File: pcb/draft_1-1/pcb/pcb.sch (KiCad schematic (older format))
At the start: 23 parts, among them J1 USB4110-GF-A, U1 H3LIS200DLTR, U2 ATSAML21G16B-AUT, U3 BQ25155

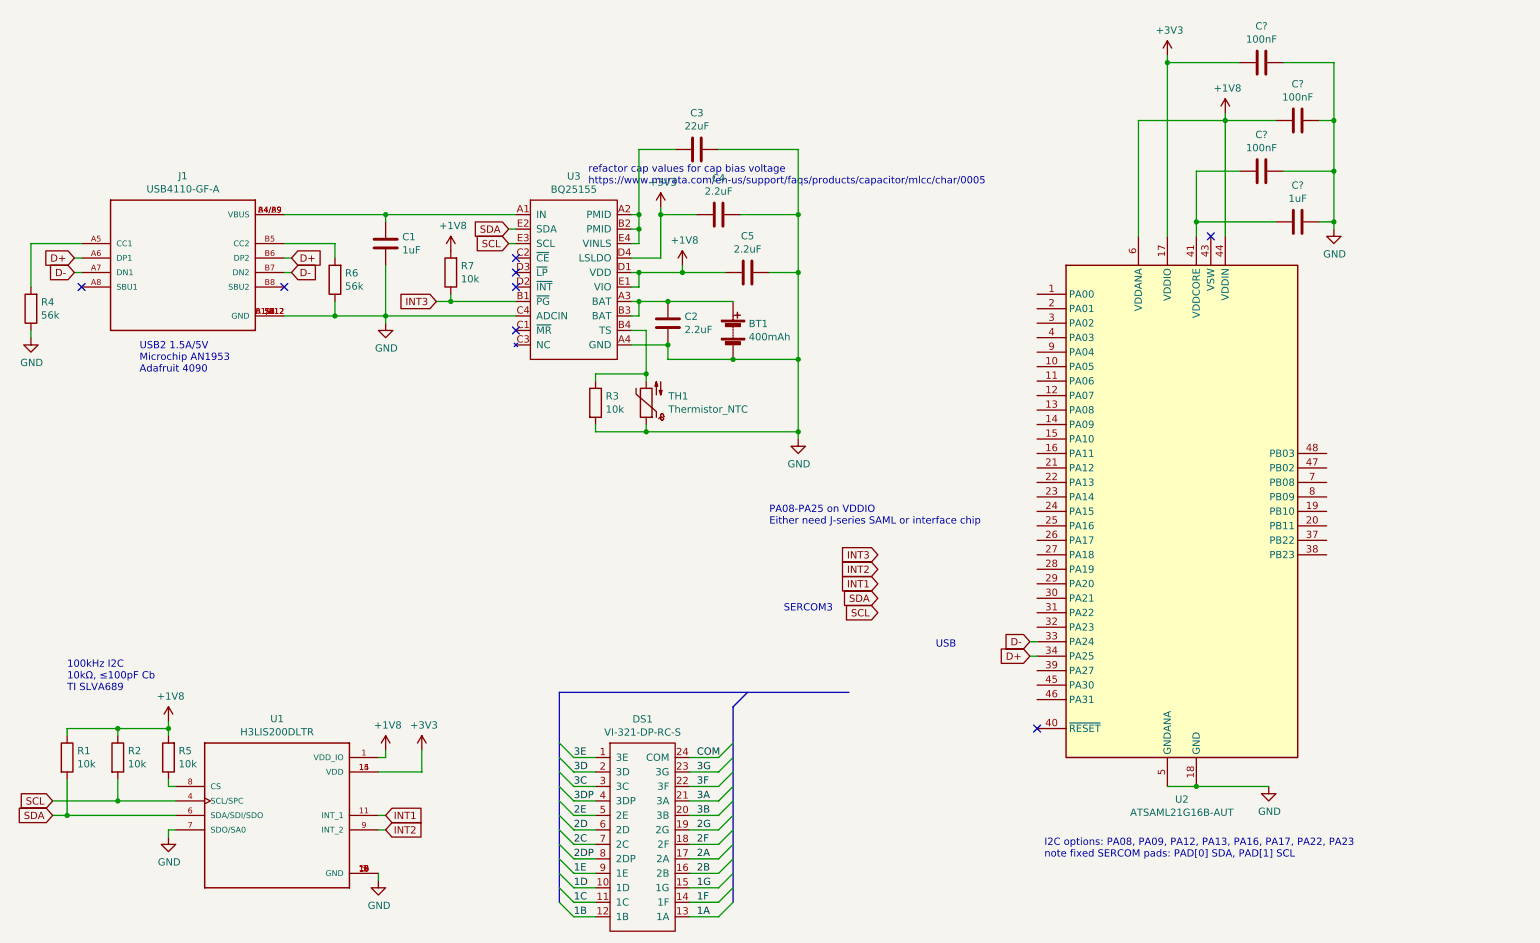
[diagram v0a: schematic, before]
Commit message: PRE-TRACE PLACEMENT CHECKPOINT
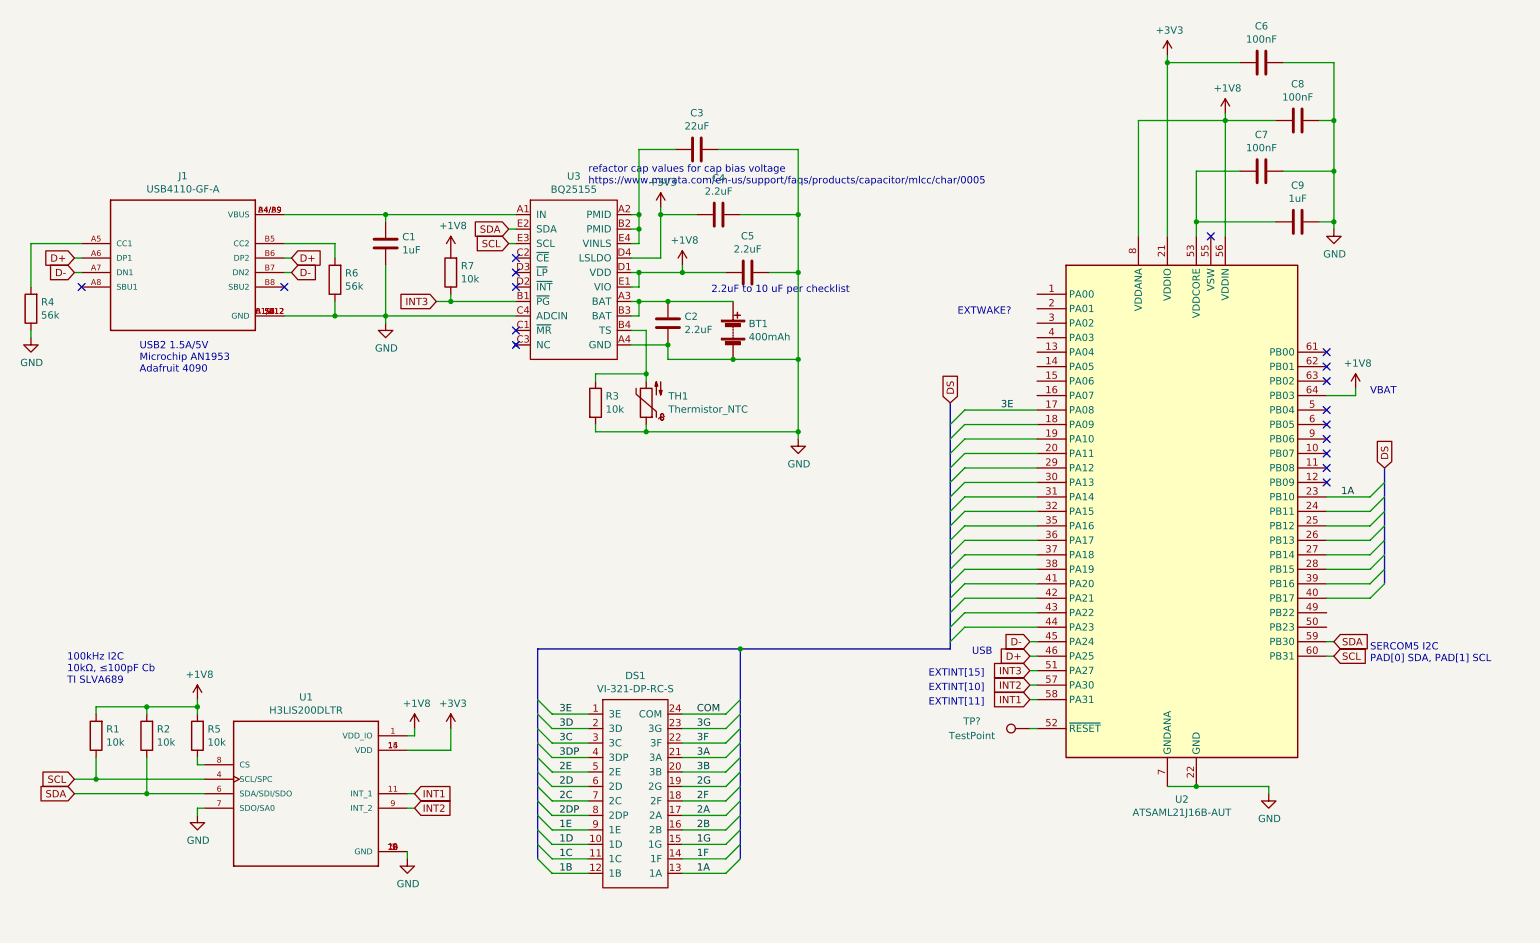
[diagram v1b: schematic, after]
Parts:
- removed U2: ATSAML21G16B-AUT, Package_QFP:TQFP-48_7x7mm_P0.5mm, symbol MCU_Microchip_SAML:ATSAML21G16B-AUT
- added TP?: TestPoint, symbol Connector:TestPoint
- added U2: ATSAML21J16B-AUT, Package_QFP:TQFP-64_10x10mm_P0.5mm, symbol MCU_Microchip_SAML:ATSAML21J16B-AUT
- DS1: footprint (none) -> custom:VI-321-DP-RC-S
- U3: footprint (none) -> SamacSys_Parts:BGA20C40P4X5_162X202X50
- gave numbers to parts that had none: 4
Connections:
- net +1V8: now also R1.2, R2.2, U2.56 (VDDIN), U2.64 (PB03), U2.8 (VDDANA); no longer R1.1, R2.1
- net +3V3: now also U2.21 (VDDIO), U2.34 (VDDIO), U2.48 (VDDIO)
- net 1A: now also U2.23 (PB10)
- net 3E: now also U2.17 (PA08)
- net D+: now also U2.46 (PA25)
- net D-: now also U2.45 (PA24)
- net GND: now also U2.22 (GND), U2.33 (GND), U2.47 (GND), U2.54 (GND), U2.7 (GNDANA)
- net INT1: now also U2.58 (PA31)
- net INT2: now also U2.57 (PA30)
- net INT3: now also U2.51 (PA27)
- net SCL: now also R1.1, U2.60 (PB31); no longer R2.2
- net SDA: now also R2.1, U2.59 (PB30); no longer R1.2
- net at C7.1, C9.1: now also U2.53 (VDDCORE)
- new net: TP?.1, U2.52 (~RESET)
- no-connect marks 8 -> 17
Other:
- note added: "2.2uF to 10 uF per checklist"
- note added: "EXTINT[10]"
- note added: "EXTINT[11]"
- note added: "EXTINT[15]"
- note added: "EXTWAKE?"
- note added: "SERCOM5 I2C\nPAD[0] SDA, PAD[1] SCL"
- note added: "VBAT"
- note removed: "I2C options: PA08, PA09, PA12, PA13, PA16, PA17, PA22, PA23\nnote fixed SERCOM pads: PAD[0] SDA, PAD[1] SCL"
- note removed: "PA08-PA25 on VDDIO\nEither need J-series SAML or interface chip"
- note removed: "SERCOM3"
- moved on the sheet: DS1, R5, U1

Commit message: attempt to route display
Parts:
- removed TP?: TestPoint, symbol Connector:TestPoint
- added L1: 10uH, Inductor_SMD:L_0805_2012Metric, symbol Device:L
- C1, C2, C3, C4, C5, C6, C7, C8, C9: footprint (none) -> Capacitor_SMD:C_0402_1005Metric
- R1, R2, R3, R4, R5, R6, R7, TH1: footprint (none) -> Resistor_SMD:R_0402_1005Metric
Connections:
- net +3V3 is gone; now on net +1V8: C4.1, C6.1, U1.14 (VDD), U1.15 (VDD), U2.21 (VDDIO), U2.34 (VDDIO), U2.48 (VDDIO), U3.D4 (LSLDO)
- net 1B is gone; now on net 24: DS1.12 (1B)
- net 1C is gone; now on net 23: DS1.11 (1C)
- net 1D is gone; now on net 22: DS1.10 (1D)
- net 1E is gone; now on net 21: DS1.9 (1E)
- net 1F is gone; now on net 2: DS1.14 (1F)
- net 1G is gone; now on net 3: DS1.15 (1G)
- net 2B is gone; now on net 4: DS1.16 (2B)
- net 2C is gone; now on net 19: DS1.7 (2C)
- net 2D is gone; now on net 18: DS1.6 (2D)
- net 2DP is gone; now on net 20: DS1.8 (2DP)
- net 2E is gone; now on net 17: DS1.5 (2E)
- net 2F is gone; now on net 6: DS1.18 (2F)
- net 2G is gone; now on net 7: DS1.19 (2G)
- net 3A is gone; now on net 9: DS1.21 (3A)
- net 3B is gone; now on net 8: DS1.20 (3B)
- net 3C is gone; now on net 15: DS1.3 (3C)
- net 3D is gone; now on net 14: DS1.2 (3D)
- net 3DP is gone; now on net 16: DS1.4 (3DP)
- net 3F is gone; now on net 10: DS1.22 (3F)
- net 3G is gone; now on net 11: DS1.23 (3G)
- net COM is gone; now on net 12: DS1.24 (COM)
- net INT1: now also U2.16 (PA07); no longer U2.58 (PA31)
- net INT2: now also U2.15 (PA06); no longer U2.57 (PA30)
- net INT3: now also U2.14 (PA05); no longer U2.51 (PA27)
- net +5V: now reaches C1.1, J1.A4/B9 (VBUS), J1.B4/A9 (VBUS), U3.A1 (IN)
- net at C7.1, C9.1, U2.53 (VDDCORE): now also L1.1
- net 2: now reaches U2.18 (PA09)
- net 3: now reaches U2.19 (PA10)
- net 4: now reaches U2.20 (PA11)
- net 6: now reaches U2.24 (PB11)
- net 7: now reaches U2.25 (PB12)
- net 8: now reaches U2.26 (PB13)
- net 9: now reaches U2.27 (PB14)
- net 10: now reaches U2.28 (PB15)
- net 11: now reaches U2.29 (PA12)
- net 12: now reaches U2.30 (PA13)
- net 13: now reaches U2.31 (PA14)
- net 13: now also DS1.1 (3E)
- net 14: now reaches U2.32 (PA15)
- net 15: now reaches U2.35 (PA16)
- net 16: now reaches U2.36 (PA17)
- net 17: now reaches U2.37 (PA18)
- net 18: now reaches U2.38 (PA19)
- net 19: now reaches U2.39 (PB16)
- net 20: now reaches U2.40 (PB17)
- net 21: now reaches U2.41 (PA20)
- net 22: now reaches U2.42 (PA21)
- net 23: now reaches U2.43 (PA22)
- net 24: now reaches U2.44 (PA23)
- net at U2.55 (VSW): now also L1.2
- net 1A renamed 1
- net 1: now also U2.17 (PA08); no longer U2.23 (PB10)
- net 2A renamed 5
- net 5: now also U2.23 (PB10)
- removed net 3E: DS1.1 (3E), U2.17 (PA08)
- no-connect marks 17 -> 27
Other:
- note added: "Buck Inductor\nAtmel AT12705"
- note added: "EXTINT[5]"
- note added: "EXTINT[6]"
- note added: "EXTINT[7]"
- note removed: "EXTINT[10]"
- note removed: "EXTINT[11]"
- note removed: "EXTINT[15]"
- moved on the sheet: BT1, C3, C4, C5, C6, C7, C8

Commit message: bom cost estimate
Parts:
- C3: footprint Capacitor_SMD:C_0402_1005Metric -> Capacitor_SMD:C_0805_2012Metric
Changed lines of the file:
@@
 F 0 "C3" V 5248 1500 50  0000 C CNN
 F 1 "22uF" V 5339 1500 50  0000 C CNN
-F 2 "Capacitor_SMD:C_0402_1005Metric" H 5538 1350 50  0001 C CNN
+F 2 "Capacitor_SMD:C_0805_2012Metric" H 5538 1350 50  0001 C CNN
 F 3 "~" H 5500 1500 50  0001 C CNN
 	1    5500 1500

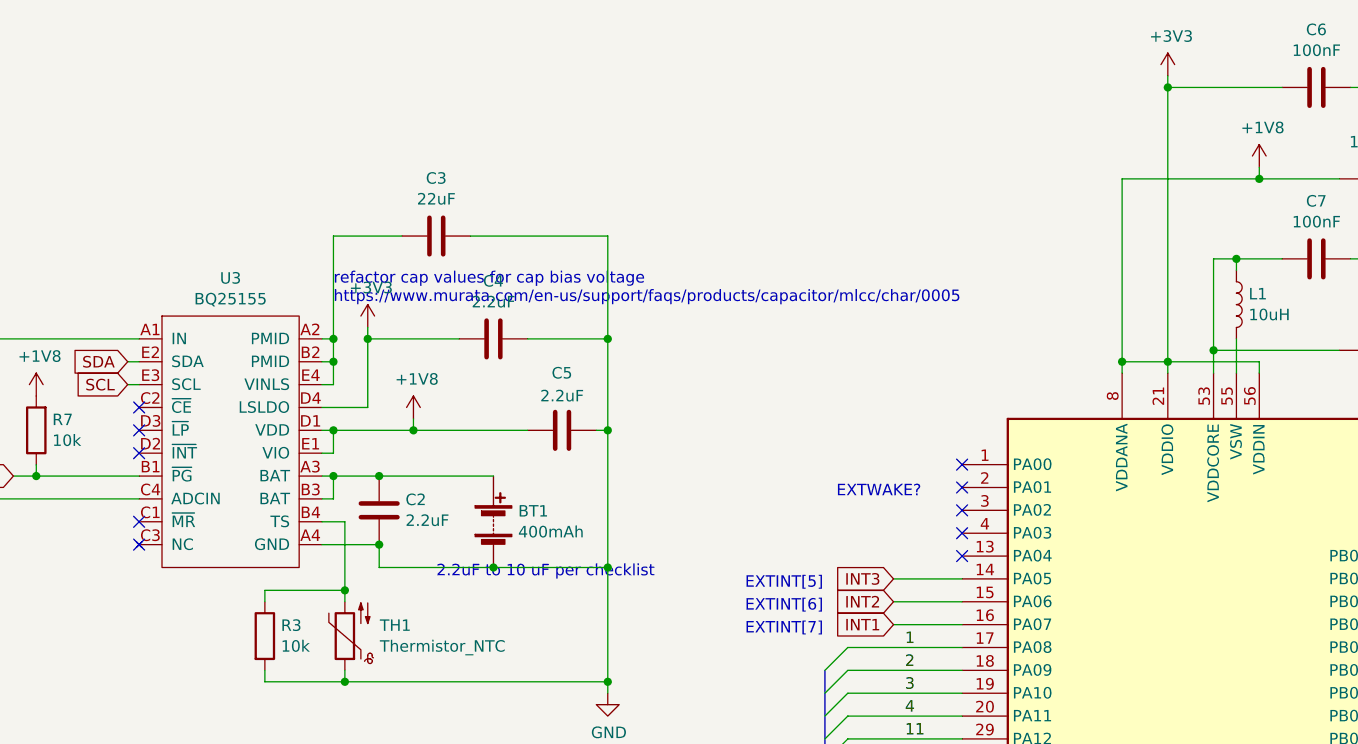
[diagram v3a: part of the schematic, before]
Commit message: maximized squid traces
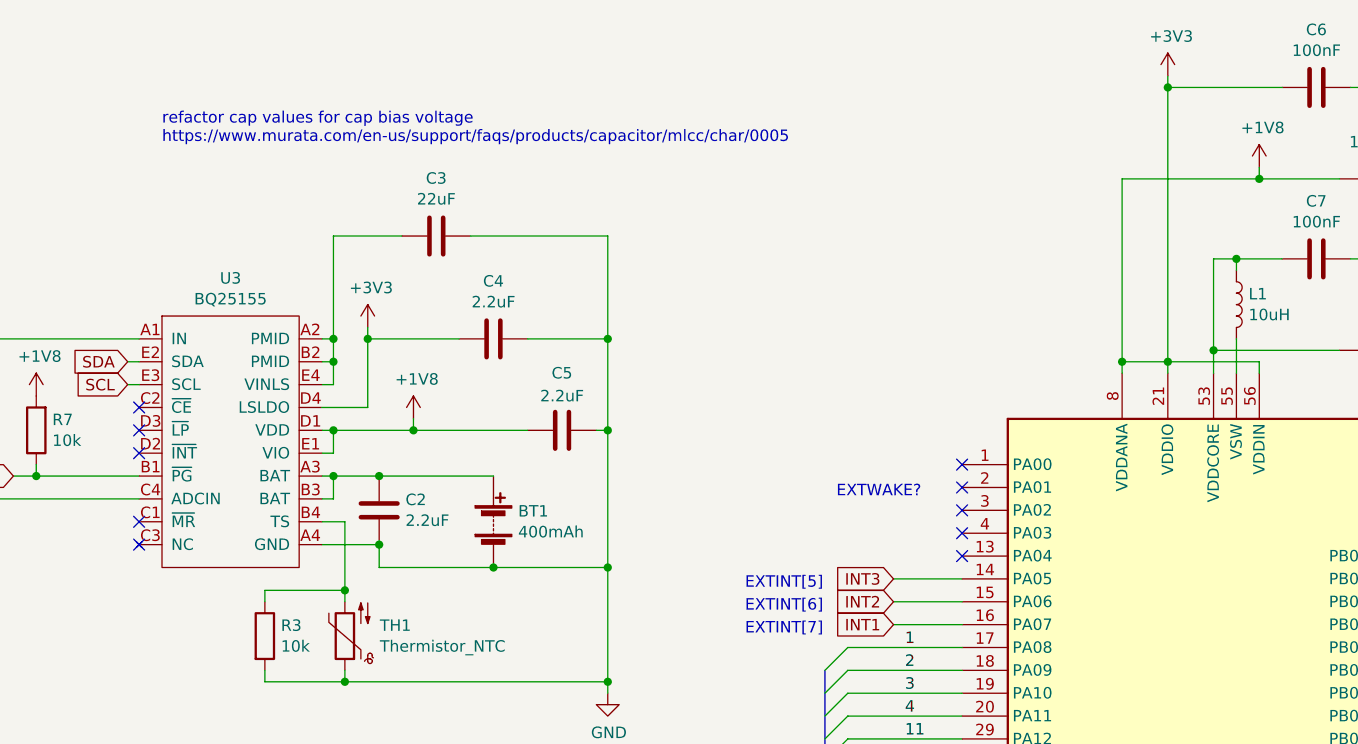
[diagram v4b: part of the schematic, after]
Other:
- note removed: "2.2uF to 10 uF per checklist"
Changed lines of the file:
@@
 Wire Wire Line
 	5050 2550 5250 2550
-Text Notes 5050 1800 0    50   ~ 0
+Text Notes 4300 1100 0    50   ~ 0
 refactor cap values for cap bias voltage\nhttps://www.murata.com/en-us/support/faqs/products/capacitor/mlcc/char/0005
 Text GLabel 3650 2550 0    50   Input ~ 0
@@
 Wire Wire Line
 	10000 3200 10000 3150
-Text Notes 5500 3000 0    50   ~ 0
-2.2uF to 10 uF per checklist
 Text Notes 10100 3200 0    50   ~ 0
 VBAT
@@
 Text Label 7550 4200 0    50   ~ 0
 16
-Text Label 7550 4300 0    50   ~ 0
-17
-Text Label 7550 4400 0    50   ~ 0
-18
 Text Label 9900 4000 0    50   ~ 0
 6
@@
 Wire Bus Line
 	7200 3400 7200 4950
+Text Label 7550 4400 0    50   ~ 0
+18
+Text Label 7550 4300 0    50   ~ 0
+17
 $EndSCHEMATC
